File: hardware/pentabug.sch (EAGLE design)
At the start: 13 parts, among them IC1 ATMEGA88

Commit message: added battery holder, bord layout changed to reflect later constellation of components
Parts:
- added BAT1: BATTERY_2XAAA, seb:BATTERY_2XAAA
- added JP2: (no value), pinhead:PINHD-2X3
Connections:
- removed net N$2: IC1.PC6(/RESET), R3.1
- new net MISO: IC1.PB4(MISO), JP2.1
- new net MOSI: IC1.PB3(MOSI/OC2), JP2.4
- new net RST: IC1.PC6(/RESET), JP2.5, R3.1
- new net SCK: IC1.PB5(SCK), JP2.3
- net GND: now also BAT1.-, JP2.6
- net VCC: now also BAT1.+
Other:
- note added: "DEFEKT!"
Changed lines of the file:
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@@
 <part name="FRAME1" library="frames" deviceset="A4L-LOC" device=""/>
 <part name="U$1" library="buglbr" deviceset="VIBRAMOTOR" device=""/>
+<part name="BAT1" library="seb" deviceset="BATTERY_2XAAA" device=""/>
+<part name="GND9" library="supply1" deviceset="GND" device=""/>
+<part name="P+3" library="supply1" deviceset="VCC" device=""/>
+<part name="JP2" library="pinhead" deviceset="PINHD-2X3" device=""/>
 </parts>
 <sheets>
@@
 <wire x1="93.98" y1="58.42" x2="205.74" y2="58.42" width="0.1524" layer="94"/>
 <text x="104.14" y="114.3" size="1.778" layer="94">Serielle Schnittsctelle</text>
+<text x="124.968" y="-43.942" size="3.81" layer="94" font="vector">DEFEKT!</text>
 </plain>
 <instances>
@@
 <instance part="FRAME1" gate="G$1" x="-50.8" y="-55.88"/>
 <instance part="U$1" gate="G$1" x="139.7" y="38.1"/>
+<instance part="BAT1" gate="G$1" x="180.34" y="2.54" rot="R90"/>
+<instance part="GND9" gate="1" x="180.34" y="-7.62" smashed="yes"/>
+<instance part="P+3" gate="VCC" x="180.34" y="12.7"/>
+<instance part="JP2" gate="A" x="180.34" y="83.82"/>
 </instances>
 <busses>
@@
 <pinref part="U$1" gate="G$1" pin="P$2"/>
 </segment>
+<segment>
+<pinref part="BAT1" gate="G$1" pin="+"/>
+<pinref part="P+3" gate="VCC" pin="VCC"/>
+<wire x1="180.34" y1="10.16" x2="180.34" y2="7.62" width="0.1524" layer="91"/>
+</segment>
 </net>
 <net name="GND" class="0">
@@
 <pinref part="Q1" gate="G$1" pin="S"/>
 <pinref part="GND1" gate="1" pin="GND"/>
+</segment>
+<segment>
+<pinref part="BAT1" gate="G$1" pin="-"/>
+<pinref part="GND9" gate="1" pin="GND"/>
+<wire x1="180.34" y1="-2.54" x2="180.34" y2="-5.08" width="0.1524" layer="91"/>
+</segment>
+<segment>
+<pinref part="JP2" gate="A" pin="6"/>
+<wire x1="185.42" y1="81.28" x2="195.58" y2="81.28" width="0.1524" layer="91"/>
+<label x="190.5" y="81.28" size="1.778" layer="95"/>
 </segment>
 </net>
@@
 </segment>
 </net>
-<net name="N$2" class="0">
-<segment>
-<wire x1="0" y1="76.2" x2="5.08" y2="76.2" width="0.1524" layer="91"/>
-<pinref part="IC1" gate="G$1" pin="PC6(/RESET)"/>
-<pinref part="R3" gate="G$1" pin="1"/>
-</segment>
-</net>
 <net name="N$3" class="0">
 <segment>
@@
 <wire x1="66.04" y1="25.4" x2="53.34" y2="25.4" width="0.1524" layer="91"/>
 <pinref part="IC1" gate="G$1" pin="PB2(SS/OC1B)"/>
+<label x="55.88" y="25.4" size="1.778" layer="95"/>
 </segment>
 </net>
@@
 </segment>
 </net>
+<net name="MISO" class="0">
+<segment>
+<pinref part="JP2" gate="A" pin="1"/>
+<wire x1="177.8" y1="86.36" x2="165.1" y2="86.36" width="0.1524" layer="91"/>
+<label x="165.1" y="86.36" size="1.778" layer="95"/>
+<label x="165.1" y="86.36" size="1.778" layer="95"/>
+</segment>
+<segment>
+<pinref part="IC1" gate="G$1" pin="PB4(MISO)"/>
+<wire x1="53.34" y1="20.32" x2="66.04" y2="20.32" width="0.1524" layer="91"/>
+<label x="55.88" y="20.32" size="1.778" layer="95"/>
+</segment>
+</net>
+<net name="SCK" class="0">
+<segment>
+<pinref part="JP2" gate="A" pin="3"/>
+<wire x1="177.8" y1="83.82" x2="165.1" y2="83.82" width="0.1524" layer="91"/>
+<label x="165.1" y="83.82" size="1.778" layer="95"/>
+</segment>
+<segment>
+<pinref part="IC1" gate="G$1" pin="PB5(SCK)"/>
+<wire x1="53.34" y1="17.78" x2="66.04" y2="17.78" width="0.1524" layer="91"/>
+<label x="55.88" y="17.78" size="1.778" layer="95"/>
+</segment>
+</net>
+<net name="RST" class="0">
+<segment>
+<pinref part="JP2" gate="A" pin="5"/>
+<wire x1="177.8" y1="81.28" x2="165.1" y2="81.28" width="0.1524" layer="91"/>
+<label x="165.1" y="81.28" size="1.778" layer="95"/>
+</segment>
+<segment>
+<wire x1="0" y1="76.2" x2="5.08" y2="76.2" width="0.1524" layer="91"/>
+<pinref part="IC1" gate="G$1" pin="PC6(/RESET)"/>
+<pinref part="R3" gate="G$1" pin="1"/>
+<label x="0" y="76.2" size="1.778" layer="95"/>
+</segment>
+</net>
+<net name="MOSI" class="0">
+<segment>
+<pinref part="JP2" gate="A" pin="4"/>
+<wire x1="185.42" y1="83.82" x2="195.58" y2="83.82" width="0.1524" layer="91"/>
+<label x="190.5" y="83.82" size="1.778" layer="95"/>
+</segment>
+<segment>
+<pinref part="IC1" gate="G$1" pin="PB3(MOSI/OC2)"/>
+<wire x1="53.34" y1="22.86" x2="66.04" y2="22.86" width="0.1524" layer="91"/>
+<label x="55.88" y="22.86" size="1.778" layer="95"/>
+</segment>
+</net>

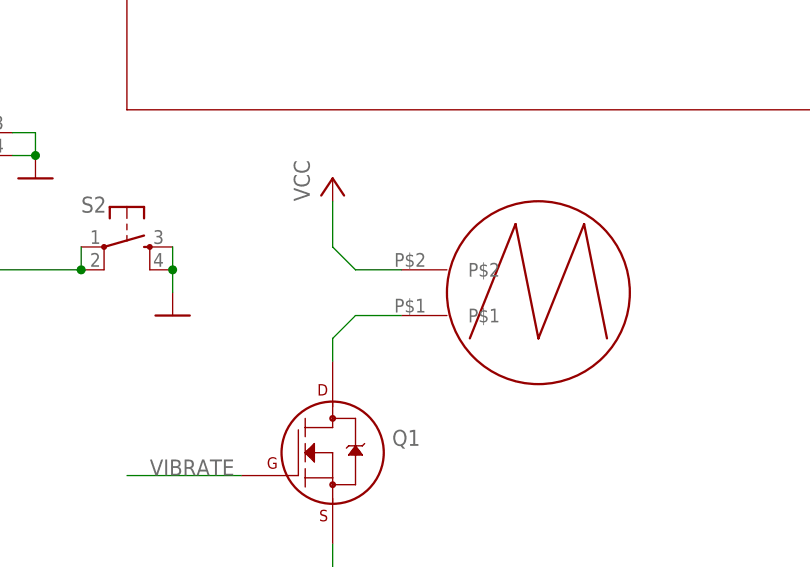
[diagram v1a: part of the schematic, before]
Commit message: some routing, buzzer footprint still wrong
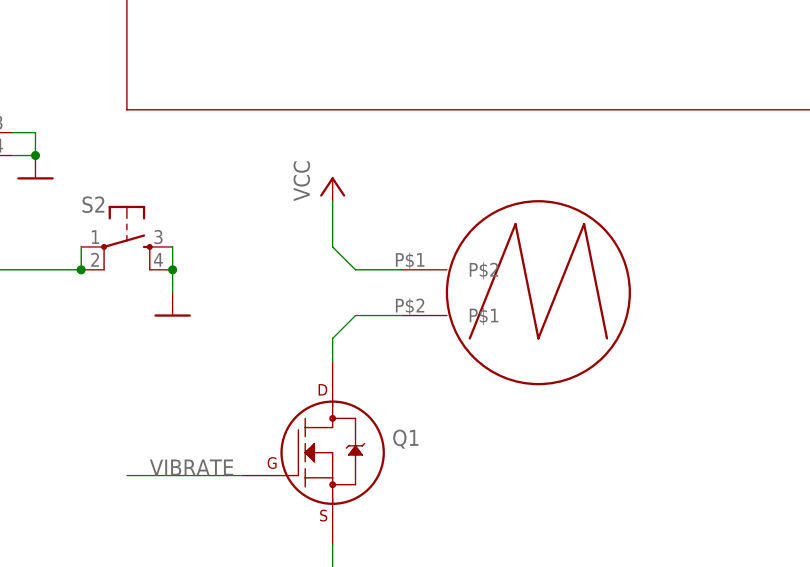
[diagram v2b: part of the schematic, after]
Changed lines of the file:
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@@
 <part name="GND3" library="supply1" deviceset="GND" device=""/>
 <part name="FRAME1" library="frames" deviceset="A4L-LOC" device=""/>
-<part name="U$1" library="buglbr" deviceset="VIBRAMOTOR" device=""/>
 <part name="BAT1" library="seb" deviceset="BATTERY_2XAAA" device=""/>
 <part name="GND9" library="supply1" deviceset="GND" device=""/>
 <part name="P+3" library="supply1" deviceset="VCC" device=""/>
 <part name="JP2" library="pinhead" deviceset="PINHD-2X3" device=""/>
+<part name="U$1" library="buglbr" deviceset="VIBRAMOTOR" device=""/>
 </parts>
 <sheets>
@@
 <instance part="GND3" gate="1" x="86.36" y="-7.62" smashed="yes"/>
 <instance part="FRAME1" gate="G$1" x="-50.8" y="-55.88"/>
-<instance part="U$1" gate="G$1" x="139.7" y="38.1"/>
 <instance part="BAT1" gate="G$1" x="180.34" y="2.54" rot="R90"/>
 <instance part="GND9" gate="1" x="180.34" y="-7.62" smashed="yes"/>
 <instance part="P+3" gate="VCC" x="180.34" y="12.7"/>
 <instance part="JP2" gate="A" x="180.34" y="83.82"/>
+<instance part="U$1" gate="G$1" x="139.7" y="38.1"/>
 </instances>
 <busses>
